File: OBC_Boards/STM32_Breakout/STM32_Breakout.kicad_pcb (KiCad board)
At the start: 4 copper layers, 95 x 95 mm, 96 parts, among them J1 Conn_02x20_Odd_Even, J2 ST1W008S4ER1500-MicroSDConnec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, J3 1050171001, J4 105017-1001, J5 1050171001, J6 SSQ-105-03-T-D, J7 SSQ-105-03-T-D, Q1 Q_PMOS_DGS, U1 MR25H10MDF, U2 BU33SA5WGWZ-E2-qsat-symb, U3 STM32L4A6ZGT6P, U4 MCP7940NT-I_MS, U5 FSM6JSMATR, U6 MCP9808

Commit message: The traces have begun
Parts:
- moved R8 118.5 mm to (29.0, 122.0)
- moved R2 115.5 mm to (29.2, 116.3)
- moved FB10 109.3 mm to (25.2, 63.7)
- moved D7 105.0 mm to (25.1, 66.3)
- moved R24 104.4 mm to (25.1, 68.3)
- moved R21 100.3 mm to (33.0, 98.0)
- moved C28 96.4 mm to (27.5, 61.3)
- moved R22 95.7 mm to (24.7, 91.9)
- moved FB8 95.2 mm to (33.0, 95.5)
- moved U1 90.7 mm to (27.9, 95.5)
- moved U6 90.3 mm to (29.1, 66.4)
- moved C23 90.0 mm to (33.3, 93.0)
- moved D4 84.8 mm to (33.2, 90.4)
- moved R19 82.6 mm to (28.5, 90.2)
- moved R10 67.3 mm to (75.6, 87.4), turned to -90 degrees
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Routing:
- net GPIO6: track 0.00 -> 86.2 mm, vias 0 -> 6
- net GPIO5: track 0.00 -> 84.0 mm, vias 0 -> 6
- net GPIO2: track 0.00 -> 55.4 mm, vias 0 -> 4
- net GPIO1: track 0.00 -> 48.7 mm, vias 0 -> 2
- net ADC12_IN16: track 0.00 -> 46.3 mm
- net GPIO16: track 0.00 -> 44.1 mm, vias 0 -> 4
- net ADC12_IN15: track 0.00 -> 43.1 mm
- net SPI2_MISO: track 0.00 -> 42.7 mm, vias 0 -> 4
- net SPI2_MOSI: track 0.00 -> 41.5 mm, vias 0 -> 2
- net GPIO15: track 0.00 -> 39.5 mm, vias 0 -> 2
- net ADC3_IN8: track 51.9 -> 90.4 mm, vias 0 -> 4
- net GPIO7: track 0.00 -> 37.2 mm, vias 0 -> 2
- net I2C1_SDA: track 0.00 -> 36.9 mm, vias 0 -> 2
- net I2C1_SCL: track 0.00 -> 36.8 mm, vias 0 -> 2
- net SPI3_NSS: track 92.2 -> 75.9 mm
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
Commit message: Small change
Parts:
- moved C17 60.9 mm to (32.0, 132.0)
- moved C13 60.9 mm to (22.6, 132.2)
- moved C14 60.9 mm to (27.0, 132.1)
- moved FB3 60.9 mm to (36.8, 132.1)
- moved C16 60.2 mm to (30.8, 138.6)
- moved C15 60.2 mm to (25.2, 138.8)
- moved FB2 60.2 mm to (35.7, 138.4)
- moved J3 47.2 mm to (123.6, 141.9), turned to 90 degrees
- moved C28 43.8 mm to (71.1, 65.2)
- moved D7 43.8 mm to (68.7, 70.2)
- moved FB10 43.8 mm to (68.8, 67.6)
- moved R24 43.8 mm to (68.7, 72.2)
- moved U6 43.8 mm to (72.7, 70.3)
- moved J5 12.2 mm to (72.3, 142.8), turned to -90 degrees
- moved TP2 8.27 mm to (155.3, 92.2)
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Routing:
- net GND: track 0.00 -> 7.14 mm, vias 0 -> 1

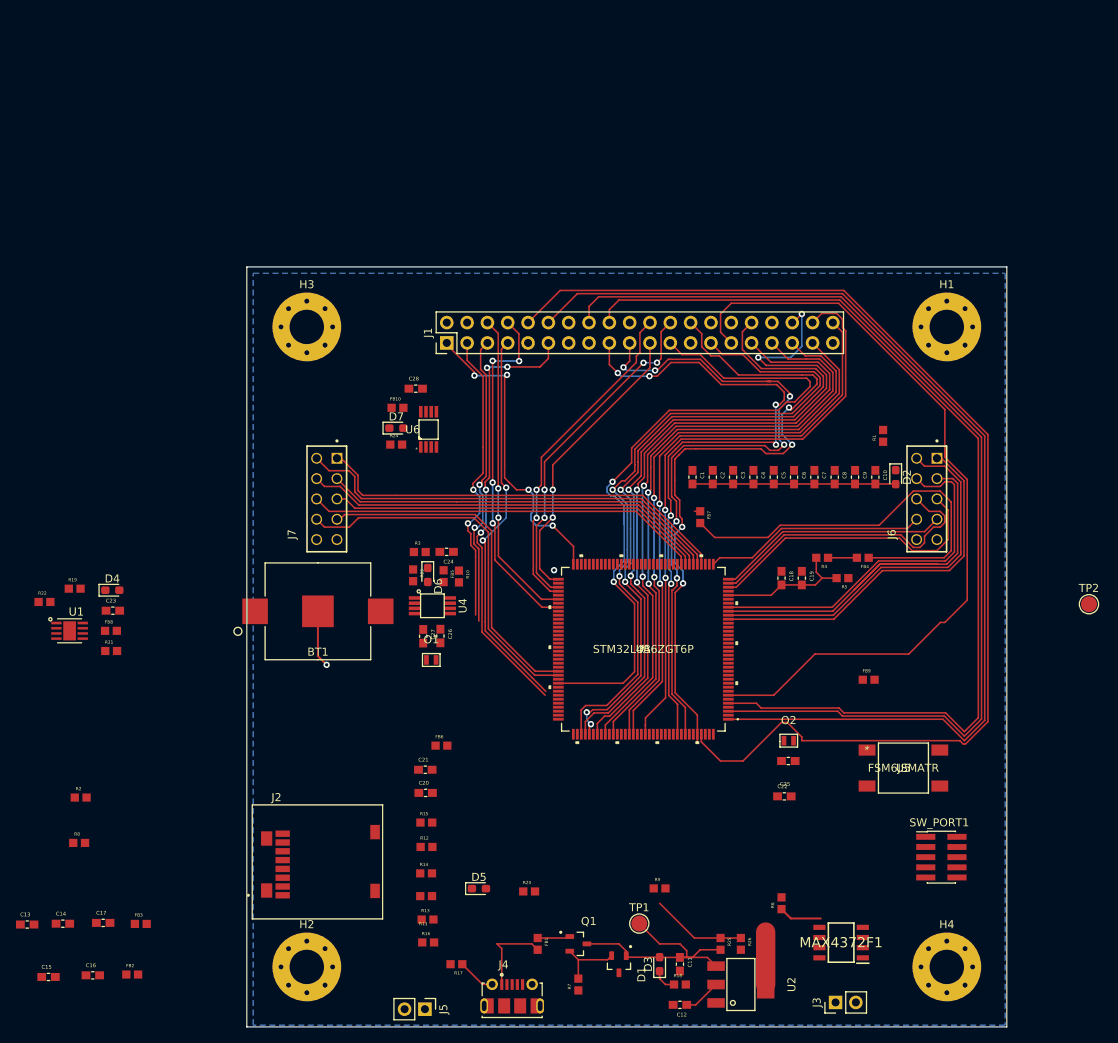
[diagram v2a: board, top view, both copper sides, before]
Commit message: Added traces to the bottom of the board
Added traces to card reader, clock and temperature sensor. Improved traces of J1. Still need to figure out trace widths of high voltage/current traces
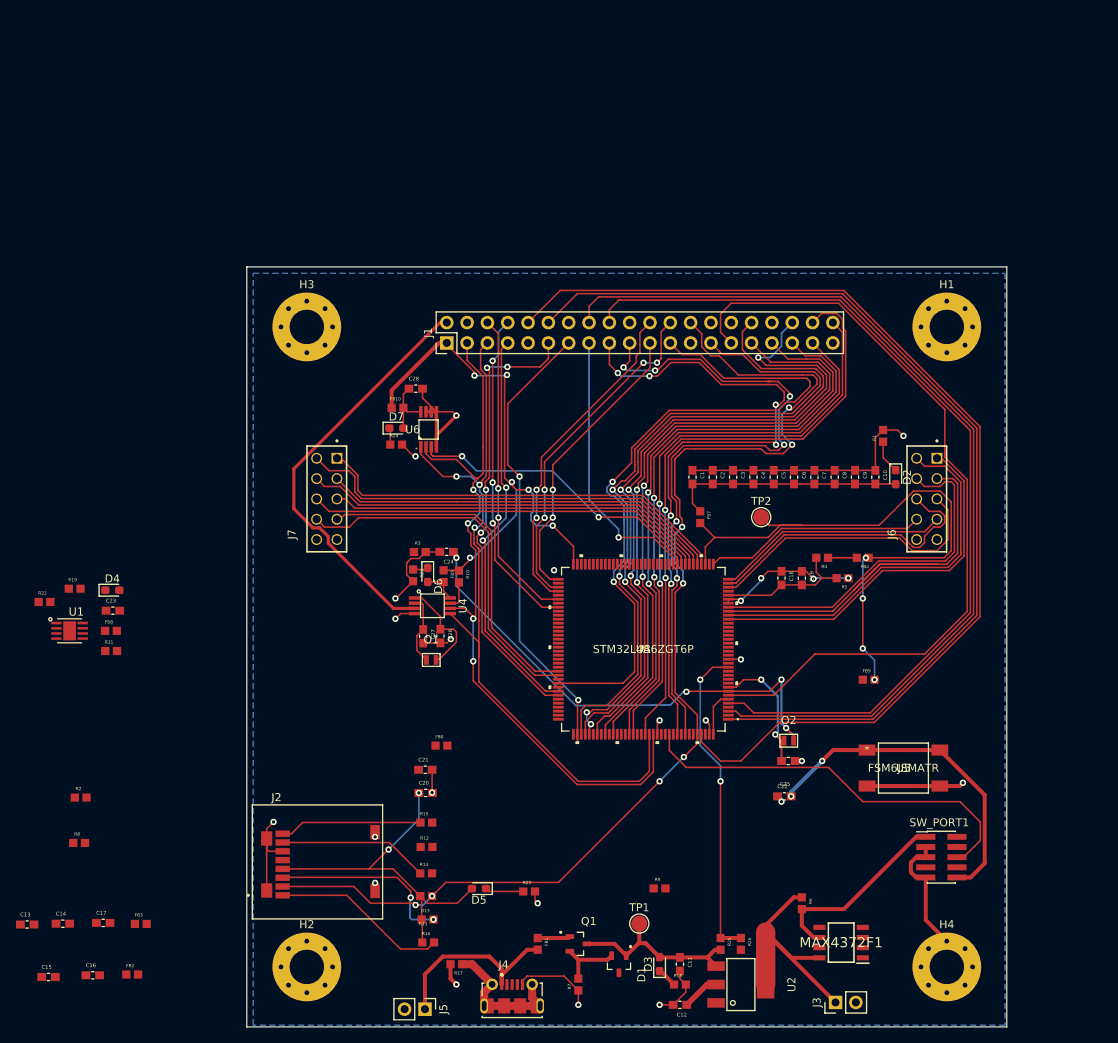
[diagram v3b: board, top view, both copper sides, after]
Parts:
- removed BT1: Battery_Cell, STM32_Breakout:36-3000-ND
- moved TP2 42.4 mm to (114.3, 81.3)
- moved R6 2.54 mm to (119.4, 129.5), turned to -90 degrees
- turned D5 to 180 degrees
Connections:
- U4 pad 3: Net-(BT1-Pad1) -> +5V
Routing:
- net GND: track 7.14 -> 140.6 mm, vias 1 -> 20
- net ADC3_IN8: track 90.4 -> 173.9 mm, vias 4 -> 10
- net SPI2_NSS: track 85.1 -> 146.3 mm, vias 4 -> 8
- net Net-(C24-Pad1): track 0.00 -> 60.8 mm, vias 0 -> 4
- net GPIO3: track 0.00 -> 56.6 mm, vias 0 -> 2
- net I2C1_SDA: track 36.9 -> 92.9 mm, vias 2 -> 3
- net I2C1_SCL: track 36.8 -> 91.0 mm, vias 2 -> 4
- net SWO: track 0.00 -> 50.7 mm
- net +5V: track 31.3 -> 75.8 mm
- net Net-(C20-Pad1): track 0.00 -> 44.2 mm, vias 0 -> 2
- net NRST: track 0.00 -> 42.0 mm, vias 0 -> 2
- net GPIOEXTI1: track 0.00 -> 37.9 mm, vias 0 -> 2
- net GPIO4: track 0.00 -> 34.6 mm, vias 0 -> 1
- net ADC3_IN7: track 12.0 -> 40.0 mm, vias 0 -> 2
- net SPI2_MOSI: track 41.5 -> 64.7 mm, vias 2 -> 4
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
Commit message: Still some connectionsleft
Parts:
- moved C15 83.8 mm to (105.6, 115.0), turned to 180 degrees
- moved R19 78.0 mm to (102.4, 65.2)
- moved C16 77.9 mm to (105.7, 117.1), turned to 180 degrees
- moved FB2 72.4 mm to (105.6, 119.5), turned to 180 degrees
- moved R2 72.1 mm to (101.3, 114.4), turned to 90 degrees
- moved R22 70.5 mm to (90.1, 65.5)
- moved R8 70.4 mm to (99.0, 114.5), turned to -90 degrees
- moved D4 69.3 mm to (97.9, 65.6), turned to 180 degrees
- moved C14 68.8 mm to (94.5, 118.6), turned to 90 degrees
- moved C13 68.8 mm to (85.9, 105.4)
- moved U1 68.2 mm to (90.8, 69.2)
- moved R21 67.8 mm to (95.4, 71.4)
- moved FB8 67.7 mm to (93.7, 65.5)
- moved C23 67.0 mm to (95.6, 68.4)
- moved C17 66.2 mm to (96.9, 118.6), turned to 90 degrees
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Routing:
- net ADC3_IN8: track 173.9 -> 283.4 mm, vias 10 -> 12
- net SPI2_CLK: track 0.00 -> 71.4 mm, vias 0 -> 6
- net SPI2_MISO: track 42.7 -> 106.6 mm, vias 4 -> 10
- net SPI2_MOSI: track 64.7 -> 123.8 mm, vias 4 -> 6
- net +5V: track 75.8 -> 26.9 mm
- net Net-(C24-Pad1): track 60.8 -> 19.9 mm, vias 4 -> 3
- net GPIO22: track 0.00 -> 36.3 mm, vias 0 -> 4
- net VDDUSB: track 0.00 -> 32.9 mm, vias 0 -> 2
- net GPIO3: track 56.6 -> 41.1 mm, vias 2 -> 1
- net GND: track 140.6 -> 125.2 mm, vias 20 -> 17
- net VDDIO2: track 0.00 -> 12.3 mm
- net Net-(C23-Pad2): track 0.00 -> 10.9 mm
- net GPIO7: track 37.2 -> 47.2 mm
- net Net-(J2-Pad8): track 17.8 -> 24.6 mm
- net SPI2_NSS: track 146.3 -> 153.0 mm
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
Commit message: First complete draft
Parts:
- moved C13 14.5 mm to (92.0, 118.6), turned to 90 degrees
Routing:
- net +5V: track 26.9 -> 139.6 mm, vias 0 -> 2
- net SWDIO: track 0.00 -> 71.7 mm, vias 0 -> 4
- net ADC3_IN6: track 0.00 -> 71.7 mm, vias 0 -> 6
- net SWCLK: track 0.00 -> 70.5 mm, vias 0 -> 2
- net Net-(FB9-Pad1): track 0.00 -> 53.7 mm, vias 0 -> 4
- net Net-(C24-Pad1): track 19.9 -> 59.0 mm, vias 3 -> 6
- net GPIO3: track 41.1 -> 69.3 mm, vias 1 -> 4
- net GPIO21: track 3.74 -> 28.9 mm, vias 0 -> 2
- net NRST: track 42.0 -> 64.7 mm, vias 2 -> 4
- net GPIO4: track 34.6 -> 54.5 mm, vias 1 -> 3
- net GND: track 125.2 -> 131.2 mm
- net VDDUSB: track 32.9 -> 27.8 mm
- net Net-(C20-Pad1): track 48.8 -> 52.7 mm
- net SPI2_MOSI: track 123.8 -> 126.1 mm
- net ADC3_IN8: track 283.4 -> 281.5 mm
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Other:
- board text added: "2021-2022 OBC Team: Jake Milley Shenghao Jin Jeremy Dube Cassidy Samoyloff Jacob Sagalovitch Kishori Kuganeswaran Harrison Gordon Armando Casanova Tomas Harmer Ivan Lipski Jillian Malherbe"

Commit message: Moved USB connector up
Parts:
- moved J4 17.9 mm to (83.8, 124.5)
- moved R11 8.60 mm to (79.8, 119.4), turned to 0 degrees
- moved R20 8.59 mm to (83.1, 114.3)
- moved D5 8.47 mm to (81.3, 116.8), turned to -90 degrees
- moved R16 6.02 mm to (76.2, 121.9), turned to -90 degrees
- moved R13 4.32 mm to (78.7, 121.9), turned to -90 degrees
- turned FB1 to 90 degrees
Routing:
- net ADC3_IN8: track 281.5 -> 325.7 mm, vias 12 -> 16
- net VDDIO2: track 12.3 -> 40.5 mm, vias 0 -> 3
- net GND: track 131.2 -> 158.8 mm, vias 17 -> 30
- net Net-(J4-PadS1): track 18.1 -> 33.4 mm
- net 5V_Input: track 24.4 -> 36.4 mm
- net Net-(C20-Pad1): track 52.7 -> 43.8 mm, vias 0 -> 2
- net Net-(J2-Pad1): track 21.1 -> 26.4 mm
- net SPI2_MOSI: track 126.1 -> 131.3 mm, vias 6 -> 7
- net Net-(D5-Pad1): track 3.47 -> 2.11 mm
- net Net-(FB1-Pad1): track 4.08 -> 4.95 mm

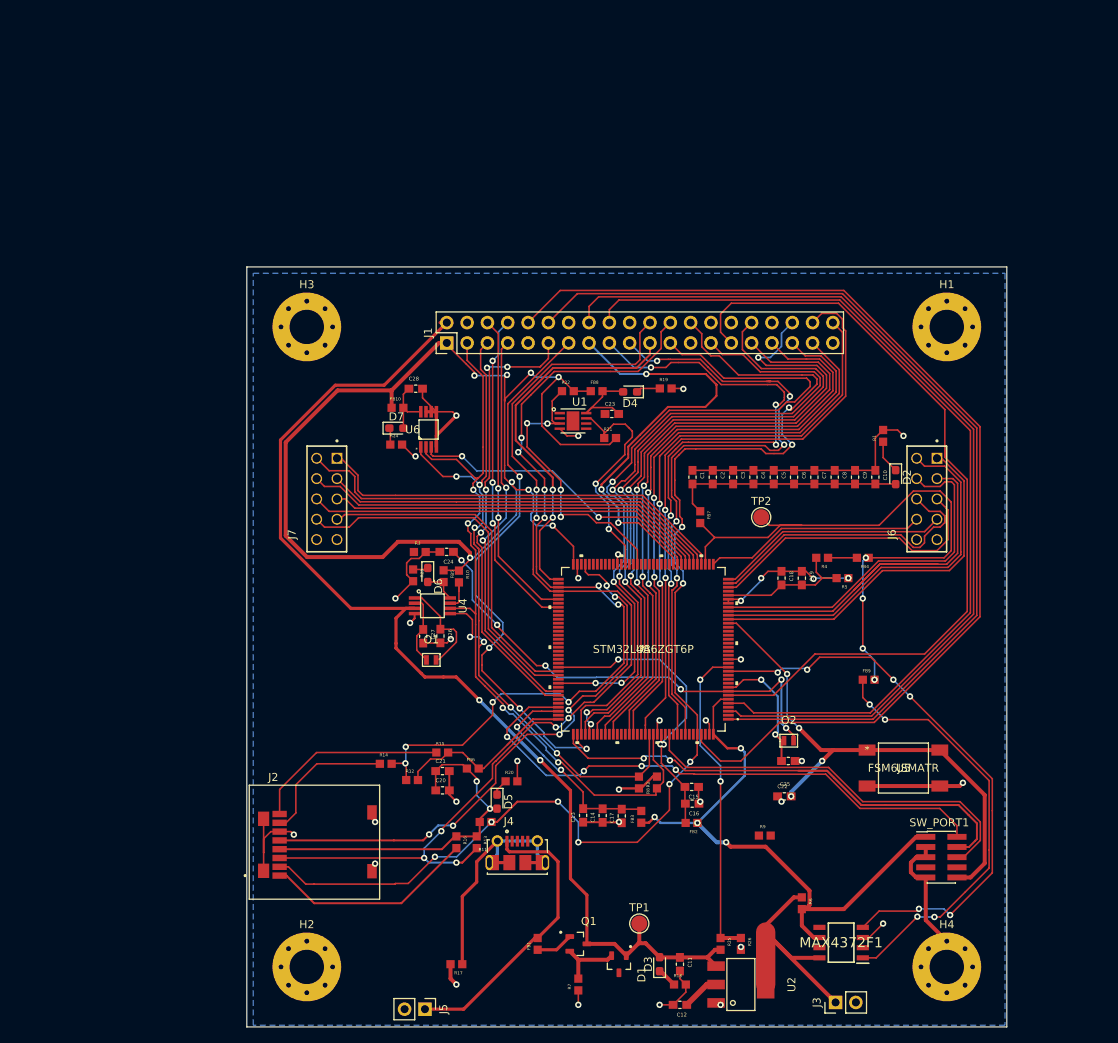
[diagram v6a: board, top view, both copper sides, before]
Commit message: Add all old footprints to new schematic Add usb input with usb-uart interfacing to provide manual commands using uart
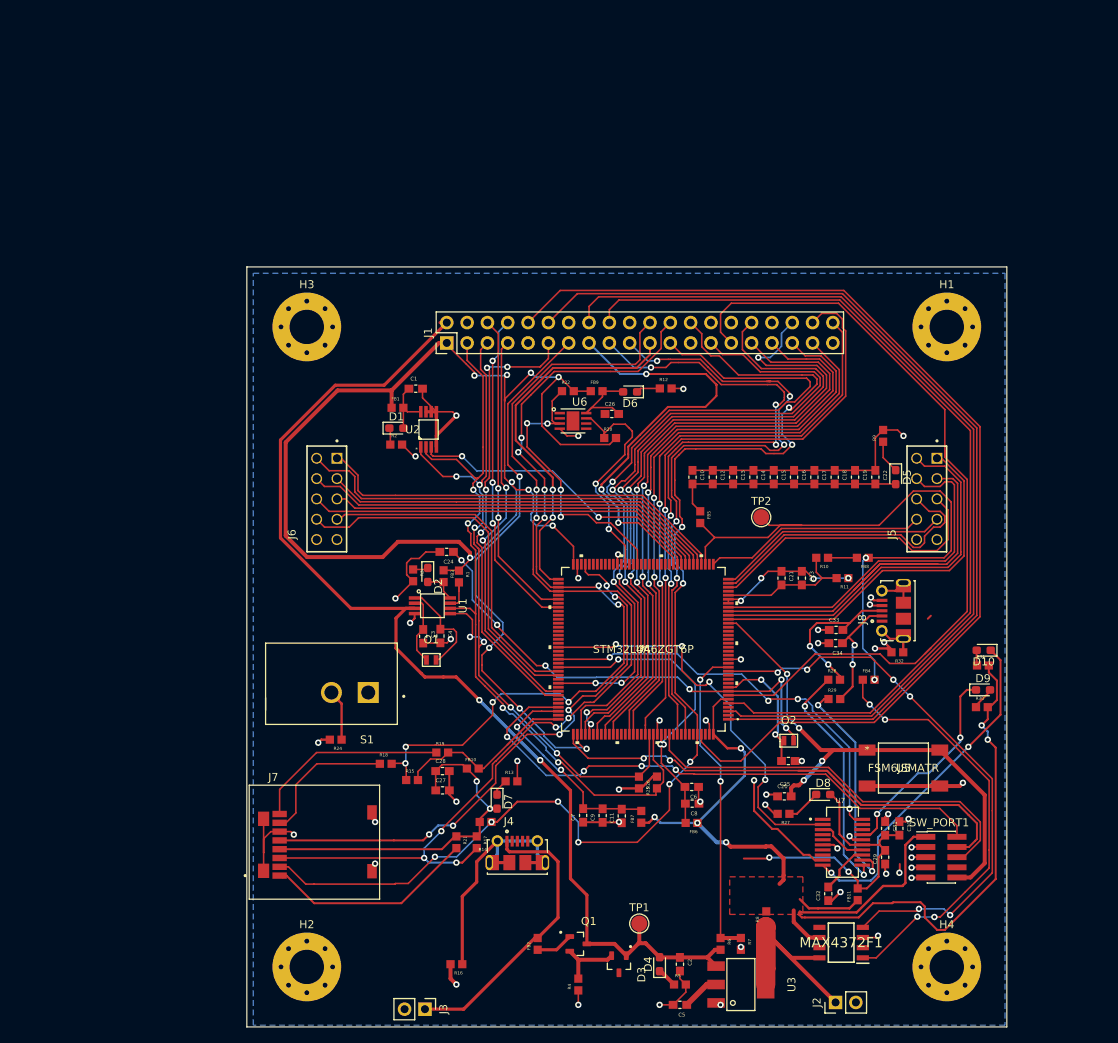
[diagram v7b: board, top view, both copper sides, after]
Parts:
- removed the R3 at (71.6, 85.6)
- removed the R9 at (114.8, 121.1)
- added C29: 4.7u, STM32_Breakout:CAPC1608X90, F.Cu at (129.8, 123.8)
- added C30: 100n, STM32_Breakout:CAPC1608X90, F.Cu at (131.6, 120.2)
- added C31: 100n, STM32_Breakout:CAPC1608X90, F.Cu at (129.8, 120.2)
- added C32: 100n, STM32_Breakout:CAPC1608X90, F.Cu at (122.7, 128.4)
- added C33: 47pF, STM32_Breakout:CAPC1608X90, F.Cu at (123.7, 95.4)
- added C34: 47pF, STM32_Breakout:CAPC1608X90, F.Cu at (123.6, 97.0)
- added D10: GREEN, LED_SMD:LED_0603_1608Metric_Pad1.05x0.95mm_HandSolder, F.Cu at (142.1, 97.9)
- added D8: RED, LED_SMD:LED_0603_1608Metric_Pad1.05x0.95mm_HandSolder, F.Cu at (122.0, 116.0)
- added D9: GREEN, LED_SMD:LED_0603_1608Metric_Pad1.05x0.95mm_HandSolder, F.Cu at (142.0, 102.9)
- added FB11: 100R @ 100 MHz, STM32_Breakout:INDUC1607X60N, F.Cu at (126.4, 128.4)
- added J8: 105017-1001, STM32_Breakout:MOLEX_105017-1001, F.Cu at (132.1, 93.0)
- added R24: 10k +-1%, STM32_Breakout:RESC1607X60N, F.Cu at (61.1, 109.1)
- added R27: 2k2, STM32_Breakout:RESC1607X60N, F.Cu at (117.1, 118.4)
- added R28: 27, STM32_Breakout:RESC1607X60N, F.Cu at (123.4, 101.6)
- added R29: 27, STM32_Breakout:RESC1607X60N, F.Cu at (123.4, 104.0)
- added R30: 2k2, STM32_Breakout:RESC1607X60N, F.Cu at (141.9, 105.0)
- added R31: 2k2, STM32_Breakout:RESC1607X60N, F.Cu at (142.0, 99.8)
- added R32: 0R, STM32_Breakout:RESC1607X60N, F.Cu at (131.3, 98.2)
- added S1: GF-123-0054, STM32_Breakout:SW_GF-123-0054, F.Cu at (60.6, 102.1)
- added U7: FT231XS-R, custom OBC footprints:SOP63P599X175-20N, F.Cu at (124.5, 121.9)
- moved R8 4.78 mm to (114.9, 131.3), turned to 90 degrees
- renumbered C28 to C1, C1 to C10, C17 to C11, C2 to C12, C3 to C13, C4 to C14, C5 to C15, C6 to C16, C7 to C17, C8 to C18, C9 to C19, C11 to C2, C22 to C20, C18 to C21, C10 to C22, C19 to C23, C23 to C26, C20 to C27, C21 to C28, C27 to C3, C26 to C4, C12 to C5, C15 to C6, C13 to C7, C16 to C8, C14 to C9, D7 to D1, D6 to D2, D1 to D3, D3 to D4, D2 to D5, D4 to D6, D5 to D7, FB10 to FB1, FB6 to FB10, FB1 to FB2, FB5 to FB3, FB9 to FB4, FB7 to FB5, FB2 to FB6, FB3 to FB7, FB4 to FB8, FB8 to FB9, J3 to J2, J5 to J3, J6 to J5, J7 to J6, J2 to J7, R10 to R1, R4 to R10, R5 to R11, R19 to R12, R20 to R13, R11 to R14, R12 to R15, R17 to R16, R13 to R17, R14 to R18, R15 to R19, R24 to R2, R21 to R20, R16 to R21, R8 to R25, R2 to R26, R23 to R3, R7 to R4, R18 to R5, R25 to R6, R26 to R7, R6 to R8, R1 to R9, U4 to U1, U6 to U2, U2 to U3, U3 to U4, U1 to U6
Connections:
- FB1 pad 1: ADC3_IN8 -> +3V3
- FB10 pad 2: ADC3_IN8 -> +3V3
- FB3 pad 1: ADC3_IN8 -> +3V3
- FB4 pad 2: ADC3_IN8 -> +3V3
- FB5 pad 2: ADC3_IN8 -> +3V3
- FB6 pad 1: ADC3_IN8 -> +3V3
- FB7 pad 1: ADC3_IN8 -> +3V3
- FB8 pad 1: ADC3_IN8 -> +3V3
- FB9 pad 1: ADC3_IN8 -> +3V3
- J1 pad 1: ADC3_IN8 -> +3V3
- J1 pad 26: SPI2_NSS -> SPI2_NSS2
- J4 pad 4: unconnected-(J4-Pad4) -> GND
- MAX4372F1 pad 6: ADC3_IN8 -> +3V3
- R1 pad 1: ADC3_IN8 -> +3V3
- R15 pad 2: ADC3_IN8 -> +3V3
- R19 pad 2: ADC3_IN8 -> +3V3
- R20 pad 2: ADC3_IN8 -> +3V3
- R22 pad 2: ADC3_IN8 -> +3V3
- R8 pad 2: ADC3_IN8 -> +3V3
- SW_PORT1 pad 1: ADC3_IN8 -> +3V3
- TP2 pad 1: ADC3_IN8 -> +3V3
- U1 pad 3: +5V -> +3V3
- U4 pad 108: ADC3_IN8 -> +3V3
- U4 pad 114: unconnected-(U3-Pad114) -> SPI2_NSS2
- U4 pad 121: ADC3_IN8 -> +3V3
- U4 pad 128: I2C1_SDA -> I2C1-SDA
- U4 pad 129: I2C1_SCL -> I2C1-SCL
- U4 pad 138: unconnected-(U3-Pad138) -> BOOT0
- U4 pad 144: ADC3_IN8 -> +3V3
- U4 pad 15: ADC3_IN8 -> +3V3
- U4 pad 17: ADC3_IN8 -> +3V3
- U4 pad 39: ADC3_IN8 -> +3V3
- U4 pad 52: ADC3_IN8 -> +3V3
- U4 pad 6: ADC3_IN8 -> +3V3
- U4 pad 62: ADC3_IN8 -> +3V3
- U4 pad 72: ADC3_IN8 -> +3V3
- U4 pad 84: ADC3_IN8 -> +3V3
- U4 pad 90: unconnected-(U3-Pad90) -> LPUART1_CTS
- U4 pad 91: unconnected-(U3-Pad91) -> LPUART1_RTS
- U4 pad 92: unconnected-(U3-Pad92) -> LPUART1_TX
- U4 pad 93: unconnected-(U3-Pad93) -> LPUART1_RX
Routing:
- net +3V3: track 0.00 -> 393.4 mm, vias 0 -> 16
- net ADC3_IN8: track 325.7 -> 0.00 mm, vias 16 -> 0
- net LPUART1_RX: track 0.00 -> 52.5 mm, vias 0 -> 4
- net LPUART1_CTS: track 0.00 -> 51.1 mm, vias 0 -> 4
- net Net-(D10-Pad1): track 0.00 -> 42.8 mm, vias 0 -> 2
- net Net-(C29-Pad2): track 0.00 -> 38.6 mm, vias 0 -> 2
- net Net-(R28-Pad1): track 0.00 -> 29.9 mm, vias 0 -> 2
- net Net-(R29-Pad1): track 0.00 -> 27.7 mm, vias 0 -> 2
- net Net-(D9-Pad1): track 0.00 -> 26.1 mm, vias 0 -> 2
- net Net-(C33-Pad2): track 0.00 -> 19.0 mm, vias 0 -> 2
- net Net-(C34-Pad1): track 0.00 -> 15.2 mm, vias 0 -> 2
- net LPUART1_RTS: track 0.00 -> 14.0 mm, vias 0 -> 1
- net GND: track 158.8 -> 171.6 mm, vias 30 -> 48
- net Net-(C32-Pad2): track 0.00 -> 12.6 mm
- net Net-(J8-PadS1): track 0.00 -> 11.0 mm
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- added copper zone on F.Cu, net +3V3
